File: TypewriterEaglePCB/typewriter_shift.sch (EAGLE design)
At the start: 39 parts, among them IC2 MDC3105LT1, U0 TPIC6A595DW, U1 TPIC6A595DW, U2 TPIC6A595DW, U3 TPIC6A595DW, U4 TPIC6A595DW, U5 TPIC6A595DW, X1 5V power

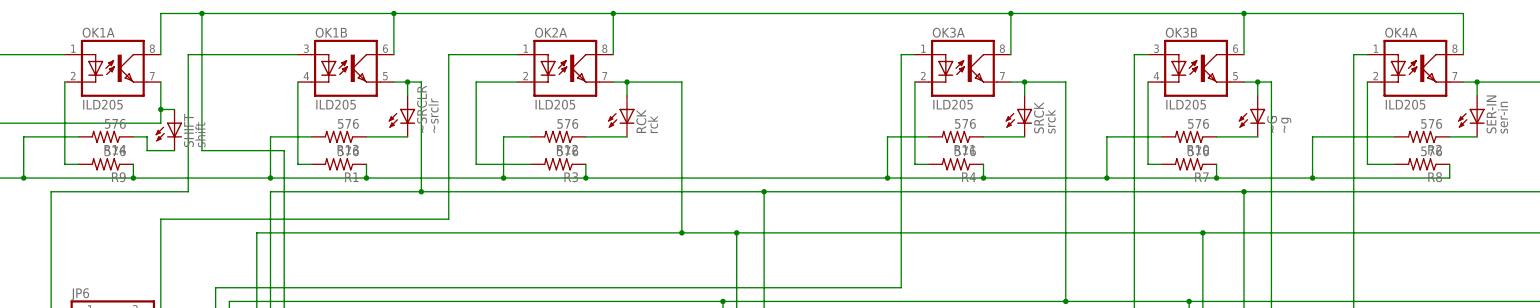
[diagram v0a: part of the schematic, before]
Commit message: Updated circuit with correct resistances for optoisolators and LEDs
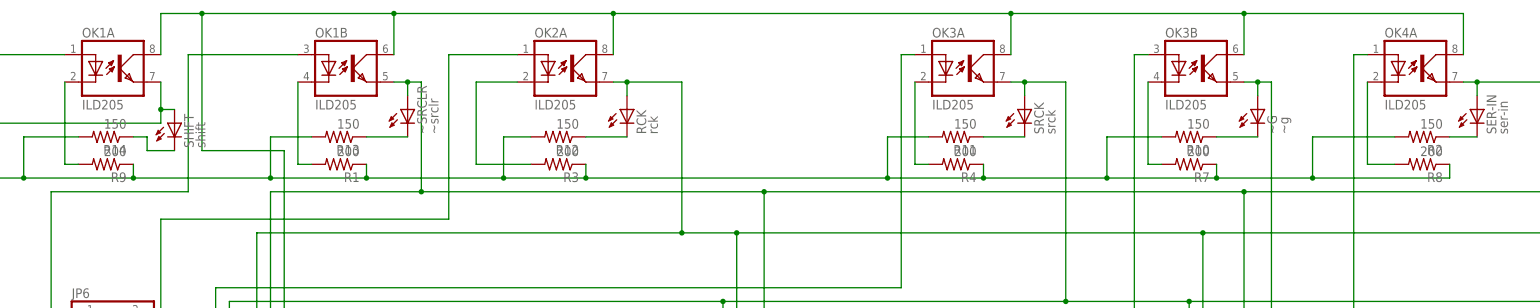
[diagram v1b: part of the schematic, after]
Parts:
- R1, R3, R4, R7, R8, R9: value 576 -> 200
- R10, R11, R12, R13, R14, R2: value 576 -> 150
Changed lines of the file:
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@@
 <part name="OK3" library="optocoupler" deviceset="ILD2*" device="" technology="05"/>
 <part name="OK4" library="optocoupler" deviceset="ILD2*" device="" technology="05"/>
-<part name="R1" library="resistor" deviceset="R-US_" device="R2512" value="576"/>
-<part name="R3" library="resistor" deviceset="R-US_" device="R2512" value="576"/>
-<part name="R4" library="resistor" deviceset="R-US_" device="R2512" value="576"/>
-<part name="R7" library="resistor" deviceset="R-US_" device="R2512" value="576"/>
-<part name="R8" library="resistor" deviceset="R-US_" device="R2512" value="576"/>
-<part name="R9" library="resistor" deviceset="R-US_" device="R2512" value="576"/>
-<part name="R2" library="resistor" deviceset="R-US_" device="R2512" value="576"/>
-<part name="R10" library="resistor" deviceset="R-US_" device="R2512" value="576"/>
-<part name="R11" library="resistor" deviceset="R-US_" device="R2512" value="576"/>
-<part name="R12" library="resistor" deviceset="R-US_" device="R2512" value="576"/>
-<part name="R13" library="resistor" deviceset="R-US_" device="R2512" value="576"/>
-<part name="R14" library="resistor" deviceset="R-US_" device="R2512" value="576"/>
+<part name="R1" library="resistor" deviceset="R-US_" device="R2512" value="200"/>
+<part name="R3" library="resistor" deviceset="R-US_" device="R2512" value="200"/>
+<part name="R4" library="resistor" deviceset="R-US_" device="R2512" value="200"/>
+<part name="R7" library="resistor" deviceset="R-US_" device="R2512" value="200"/>
+<part name="R8" library="resistor" deviceset="R-US_" device="R2512" value="200"/>
+<part name="R9" library="resistor" deviceset="R-US_" device="R2512" value="200"/>
+<part name="R2" library="resistor" deviceset="R-US_" device="R2512" value="150"/>
+<part name="R10" library="resistor" deviceset="R-US_" device="R2512" value="150"/>
+<part name="R11" library="resistor" deviceset="R-US_" device="R2512" value="150"/>
+<part name="R12" library="resistor" deviceset="R-US_" device="R2512" value="150"/>
+<part name="R13" library="resistor" deviceset="R-US_" device="R2512" value="150"/>
+<part name="R14" library="resistor" deviceset="R-US_" device="R2512" value="150"/>
 <part name="RCK" library="led" deviceset="LED" device="SML1206" value="rck"/>
 <part name="~SRCLR" library="led" deviceset="LED" device="SML1206" value="~srclr"/>

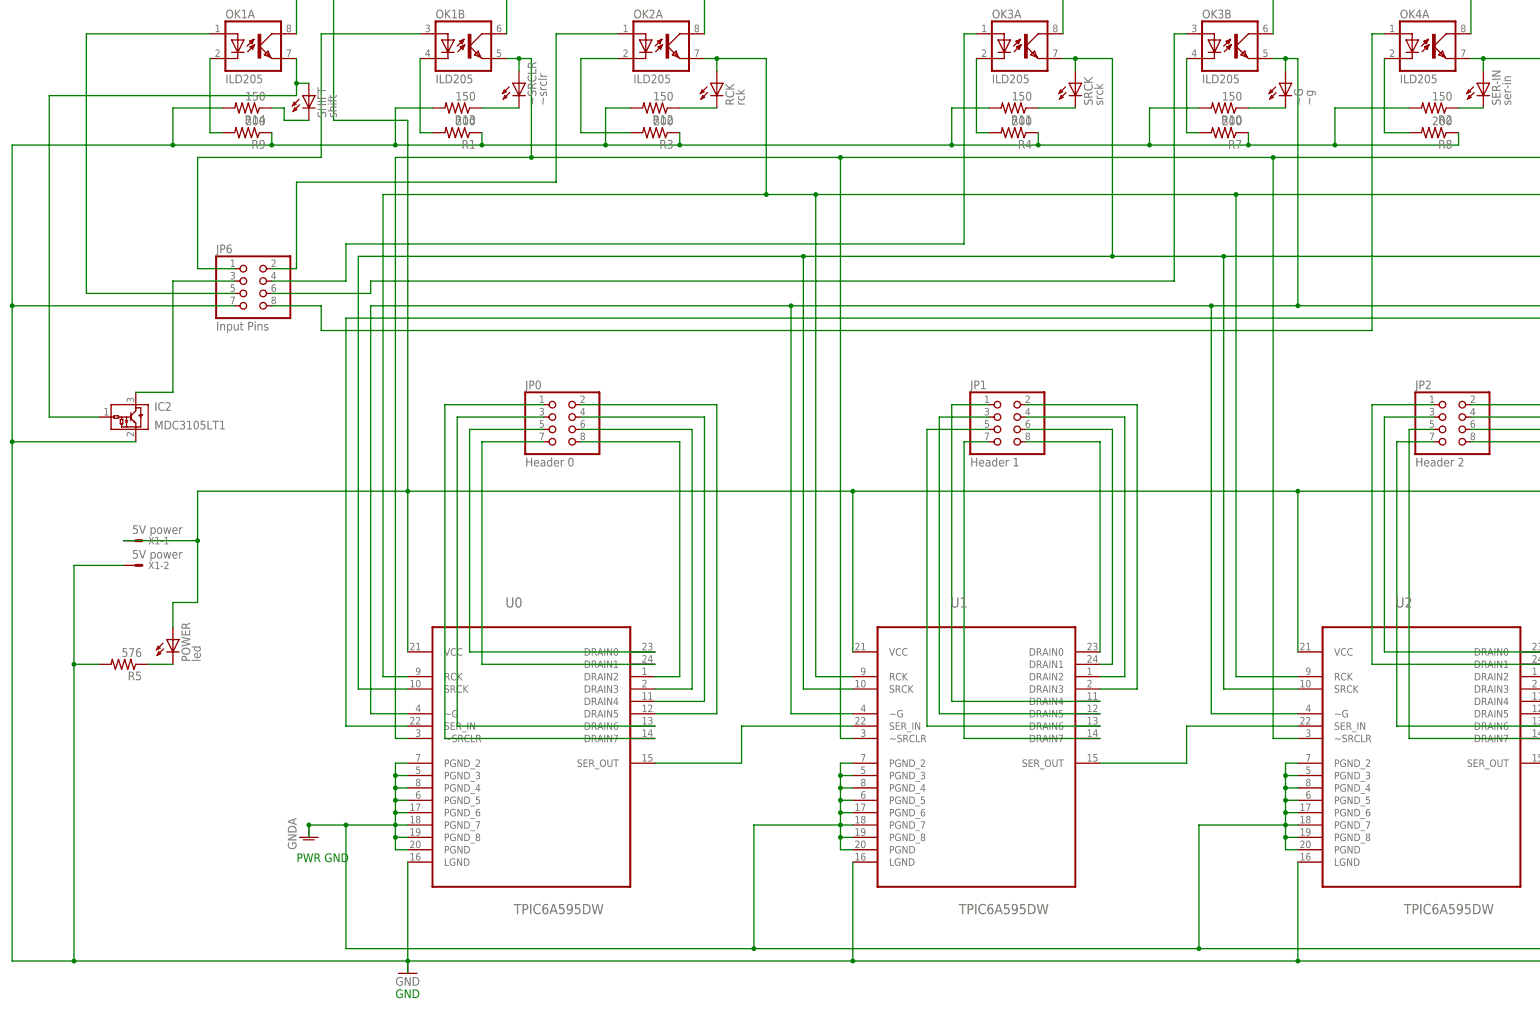
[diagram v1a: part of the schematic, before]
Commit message: Added wide power ground traces and 1206 resistors
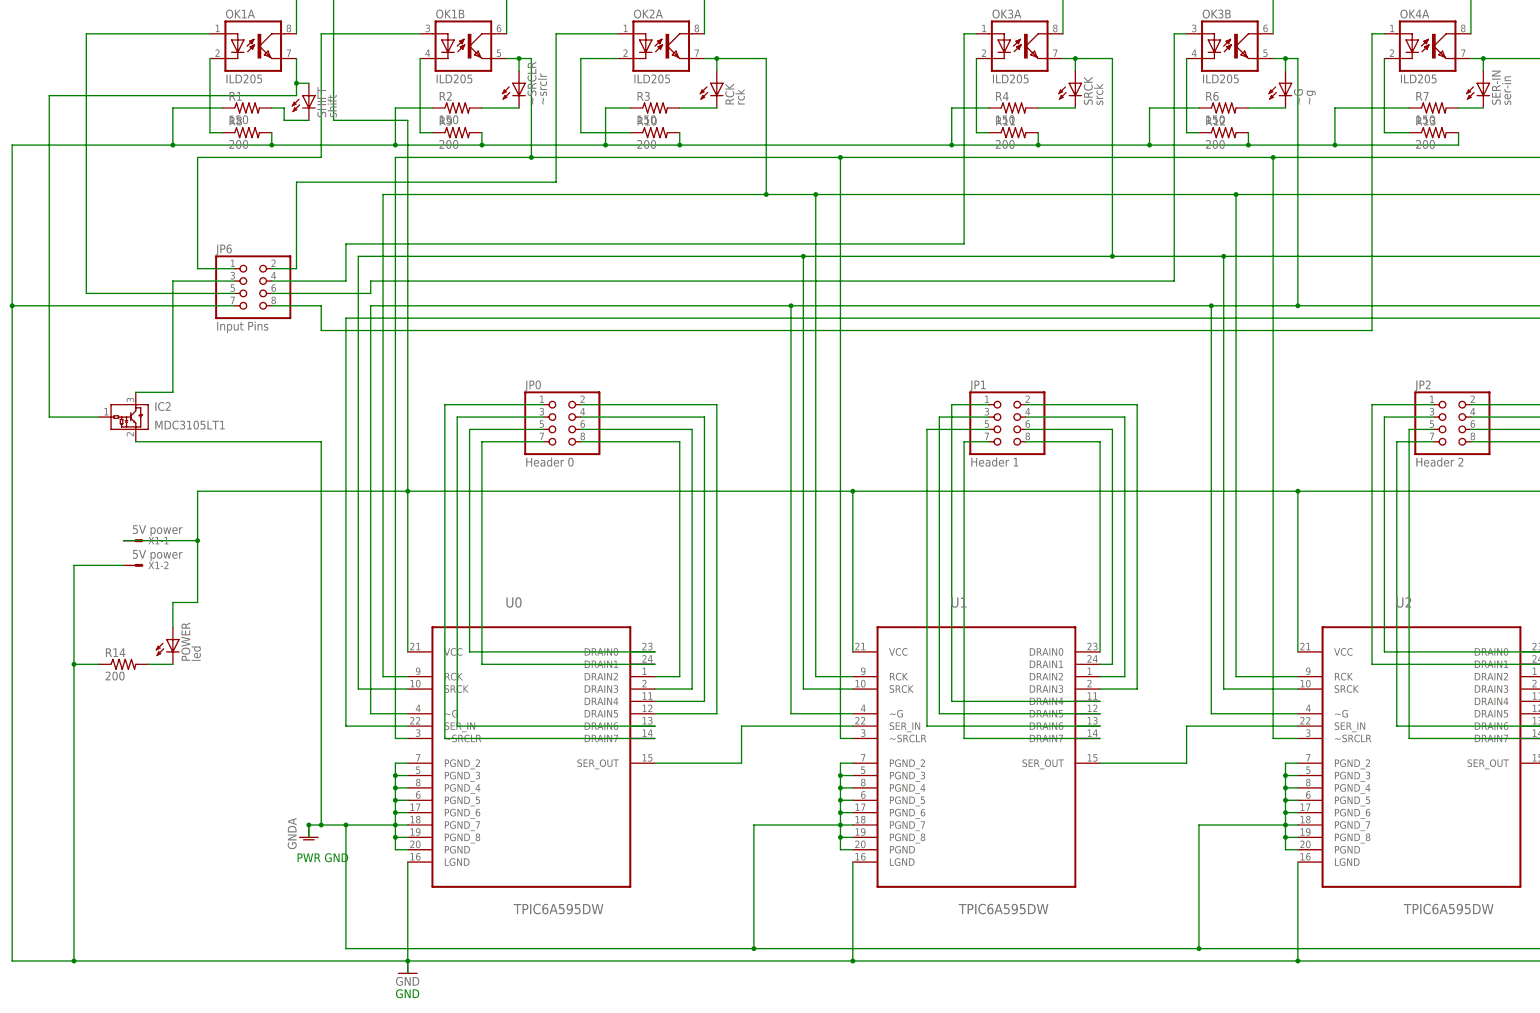
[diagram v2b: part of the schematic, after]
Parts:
- removed R5: 576, resistor:R-US_R2512
- added R6: 150, resistor:R-US_R1206
- R1, R3, R4, R7: value 200 -> 150; device resistor:R-US_R2512 -> resistor:R-US_R1206
- R10, R11, R12, R13, R14: value 150 -> 200; device resistor:R-US_R2512 -> resistor:R-US_R1206
- R2, R8, R9: device resistor:R-US_R2512 -> resistor:R-US_R1206
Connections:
- net GND: now also R14.1, R2.1, R6.1, R8.2, R9.2; no longer IC2.GND, R14.2, R2.2, R5.2, R8.1, R9.1
- net GNDA: now also IC2.GND
- net N$17: now also R8.1; no longer R9.2
- net N$32: now also R12.1; no longer R7.2
- net N$6: now also R3.2; no longer R12.1
- net N$72: now also R13.1; no longer R8.2
- net N$73: now also R1.2; no longer R14.1
- net N$74: now also R4.2; no longer R11.1
- net N$75: now also R6.2; no longer R10.1
- net N$76: now also R11.1; no longer R4.2
- net N$77: now also R10.1; no longer R3.2
- net N$78: now also R9.1; no longer R1.2
- net N$79: now also R7.2; no longer R2.1
- net N$8: now also R2.2; no longer R13.1
- net N$80: now also R14.2; no longer R5.1
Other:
- moved on the sheet: R1, R10, R11, R12, R13, R14, R2, R3, R4, R7, R8, R9
